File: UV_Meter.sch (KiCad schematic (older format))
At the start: 8 parts, among them SW1 SW_Push, U1 ATtiny85-20PU

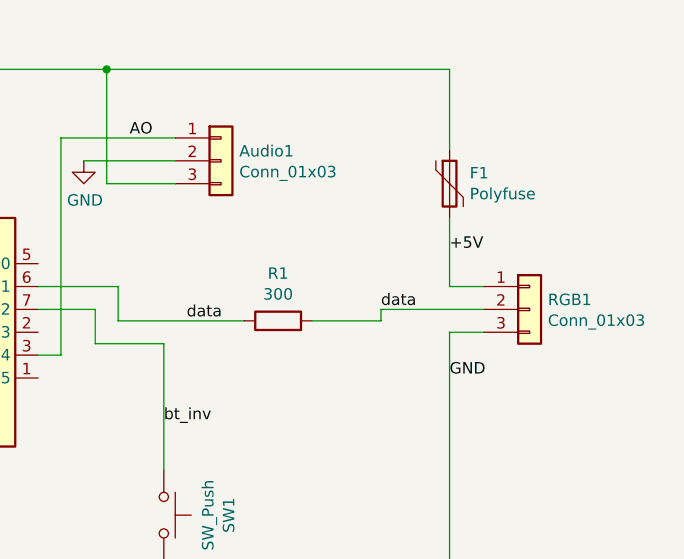
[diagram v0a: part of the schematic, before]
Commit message: switched PWR & LED
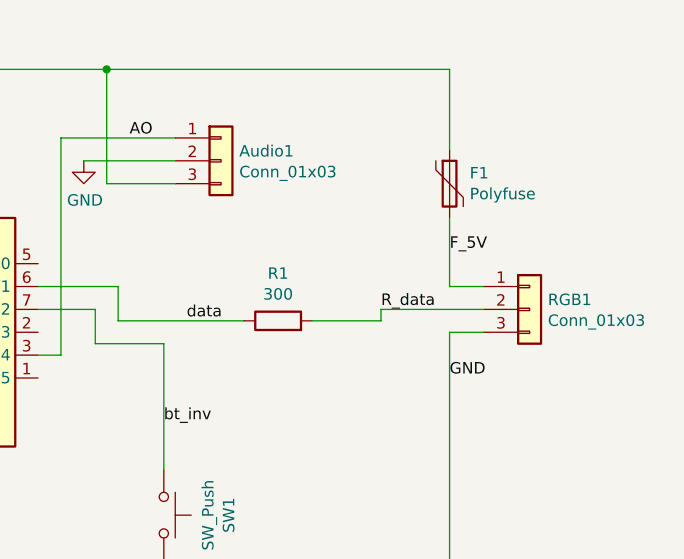
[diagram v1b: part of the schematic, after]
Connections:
- net +5V: no longer F1.2, RGB1.1 (Pin_1)
- net data: no longer R1.2, RGB1.2 (Pin_2)
- new net F_5V: F1.2, RGB1.1 (Pin_1)
- new net R_data: R1.2, RGB1.2 (Pin_2)
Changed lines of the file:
@@
 $EndComp
-Wire Wire Line
-	4550 2650 4850 2650
 Wire Wire Line
 	4850 2650 4850 2600
@@
 	4850 2600 5300 2600
 Text Label 4850 2600 0    50   ~ 0
-data
+R_data
 Text Label 5150 2350 0    50   ~ 0
-+5V
+F_5V
 Text Label 5150 2900 0    50   ~ 0
 GND
@@
 Wire Wire Line
 	5150 2200 5150 2500
-Wire Wire Line
-	5150 1550 5150 1900
 $Comp
 L Device:Polyfuse F1
@@
 	1    0    0    -1
 $EndComp
+Wire Wire Line
+	5150 1550 5150 1900
+Wire Wire Line
+	4850 2650 4550 2650
 $EndSCHEMATC

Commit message: added mounting holes and played around
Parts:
- added H1: MountingHole, MountingHole:MountingHole_3.2mm_M3_ISO14580, symbol Mechanical:MountingHole
- added R_reset1: 10k, Resistor_SMD:R_0603_1608Metric, symbol Device:R
- F_LED1: renamed from F1; value Polyfuse -> 500mA
- renumbered R1 to R_data1
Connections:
- net +5V: now also R_reset1.1
- net reset: now reaches U1.1 (~RESET~/PB5)
- net reset: now also R_reset1.2
- net F_5V renamed fused_5V
- net R_data renamed r_data
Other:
- moved on the sheet: C1
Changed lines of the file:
@@
 $EndComp
 $Comp
-L Device:R R1
+L Device:R R_data1
 U 1 1 5C9F3835
 P 4400 2650
-F 0 "R1" V 4607 2650 50  0000 C CNN
+F 0 "R_data1" V 4607 2650 50  0000 C CNN
 F 1 "300" V 4516 2650 50  0000 C CNN
 F 2 "Resistor_SMD:R_0603_1608Metric" V 4330 2650 50  0001 C CNN
@@
 	4850 2600 5300 2600
 Text Label 4850 2600 0    50   ~ 0
-R_data
+r_data
 Text Label 5150 2350 0    50   ~ 0
-F_5V
+fused_5V
 Text Label 5150 2900 0    50   ~ 0
 GND
 Wire Wire Line
-	5150 1550 3650 1550
-Wire Wire Line
 	5150 2200 5150 2500
 $Comp
-L Device:Polyfuse F1
+L Device:Polyfuse F_LED1
 U 1 1 5CA0A446
 P 5150 2050
-F 0 "F1" H 5238 2096 50  0000 L CNN
-F 1 "Polyfuse" H 5238 2005 50  0000 L CNN
+F 0 "F_LED1" H 5238 2096 50  0000 L CNN
+F 1 "500mA" H 5238 2005 50  0000 L CNN
 F 2 "Fuse:Fuse_1206_3216Metric" H 5200 1850 50  0001 L CNN
 F 3 "~" H 5150 2050 50  0001 C CNN
@@
 	1900 3400 2750 3400
 Wire Wire Line
-	1900 2450 1900 3400
-Wire Wire Line
-	1900 2150 1900 2050
+	1900 2650 1900 3400
+Wire Wire Line
+	1900 2350 1900 2050
 Wire Wire Line
 	1900 2050 2750 2050
@@
 bt_inv
 Wire Wire Line
-	3700 2650 4250 2650
+	3900 2650 4250 2650
 Text Label 4000 2650 0    50   ~ 0
 data
-Text Label 3750 1850 0    50   ~ 0
-AO
-$Comp
-L power:GND #PWR0103
-U 1 1 5CA39264
-P 3550 1950
-F 0 "#PWR0103" H 3550 1700 50  0001 C CNN
-F 1 "GND" H 3555 1777 50  0000 C CNN
-F 2 "" H 3550 1950 50  0001 C CNN
-F 3 "" H 3550 1950 50  0001 C CNN
-	1    3550 1950
-	1    0    0    -1
-$EndComp
-Wire Wire Line
-	3950 1950 3550 1950
-Wire Wire Line
-	3950 2050 3650 2050
-Wire Wire Line
-	3650 2050 3650 1550
-Connection ~ 3650 1550
-Wire Wire Line
-	3650 1550 2750 1550
-Wire Wire Line
-	3350 2800 3450 2800
-Wire Wire Line
-	3450 2800 3450 1850
-Wire Wire Line
-	3450 1850 3950 1850
+Wire Wire Line
+	3350 2800 3700 2800
 $Comp
 L Device:C C1
 U 1 1 5C9F146E
-P 1900 2300
-F 0 "C1" H 2015 2346 50  0000 L CNN
-F 1 "100u" H 2015 2255 50  0000 L CNN
-F 2 "Capacitor_THT:CP_Radial_D7.5mm_P2.50mm" H 1938 2150 50  0001 C CNN
-F 3 "~" H 1900 2300 50  0001 C CNN
-	1    1900 2300
+P 1900 2500
+F 0 "C1" H 2015 2546 50  0000 L CNN
+F 1 "100u" H 2015 2455 50  0000 L CNN
+F 2 "Capacitor_THT:CP_Radial_D7.5mm_P2.50mm" H 1938 2350 50  0001 C CNN
+F 3 "~" H 1900 2500 50  0001 C CNN
+	1    1900 2500
 	1    0    0    -1
 $EndComp
@@
 	1450 2750 1450 4000
 Wire Wire Line
-	3700 2500 3350 2500
-Wire Wire Line
-	3700 2500 3700 2650
-Wire Wire Line
-	3350 2600 3600 2600
-Wire Wire Line
-	3600 2600 3600 2750
-Wire Wire Line
-	3600 2750 3900 2750
+	3900 2500 3350 2500
+Wire Wire Line
+	3900 2500 3900 2650
+Wire Wire Line
+	3350 2600 3800 2600
+Wire Wire Line
+	3800 2600 3800 2750
+Wire Wire Line
+	3800 2750 3900 2750
 Wire Wire Line
 	3900 2750 3900 3300
+Wire Wire Line
+	5150 1550 5150 1900
+Wire Wire Line
+	4850 2650 4550 2650
+$Comp
+L Device:R R_reset1
+U 1 1 5CA11B10
+P 3100 2050
+F 0 "R_reset1" V 3307 2050 50  0000 C CNN
+F 1 "10k" V 3216 2050 50  0000 C CNN
+F 2 "Resistor_SMD:R_0603_1608Metric" V 3030 2050 50  0001 C CNN
+F 3 "~" H 3100 2050 50  0001 C CNN
+	1    3100 2050
+	0    -1   -1   0
+$EndComp
+Wire Wire Line
+	2750 2050 2950 2050
+Wire Wire Line
+	3250 2050 3450 2050
+Wire Wire Line
+	3450 2050 3450 2900
+Wire Wire Line
+	3450 2900 3350 2900
+Connection ~ 3900 1550
+Wire Wire Line
+	3900 1550 2750 1550
+Wire Wire Line
+	5150 1550 3900 1550
 $Comp
 L Connector_Generic:Conn_01x03 Audio1
@@
 $EndComp
 Wire Wire Line
-	5150 1550 5150 1900
-Wire Wire Line
-	4850 2650 4550 2650
+	3700 1850 3950 1850
+Wire Wire Line
+	3700 2800 3700 1850
+Wire Wire Line
+	3900 2050 3900 1550
+Wire Wire Line
+	3950 2050 3900 2050
+Wire Wire Line
+	3950 1950 3750 1950
+$Comp
+L power:GND #PWR0103
+U 1 1 5CA39264
+P 3750 1950
+F 0 "#PWR0103" H 3750 1700 50  0001 C CNN
+F 1 "GND" H 3755 1777 50  0000 C CNN
+F 2 "" H 3750 1950 50  0001 C CNN
+F 3 "" H 3750 1950 50  0001 C CNN
+	1    3750 1950
+	1    0    0    -1
+$EndComp
+Text Label 3750 1850 0    50   ~ 0
+AO
+Text Label 3350 2050 0    50   ~ 0
+reset
+$Comp
+L Mechanical:MountingHole H1
+U 1 1 5CA3BE5F
+P 5250 1300
+F 0 "H1" H 5350 1346 50  0000 L CNN
+F 1 "MountingHole" H 5350 1255 50  0000 L CNN
+F 2 "MountingHole:MountingHole_3.2mm_M3_ISO14580" H 5250 1300 50  0001 C CNN
+F 3 "~" H 5250 1300 50  0001 C CNN
+	1    5250 1300
+	1    0    0    -1
+$EndComp
 $EndSCHEMATC

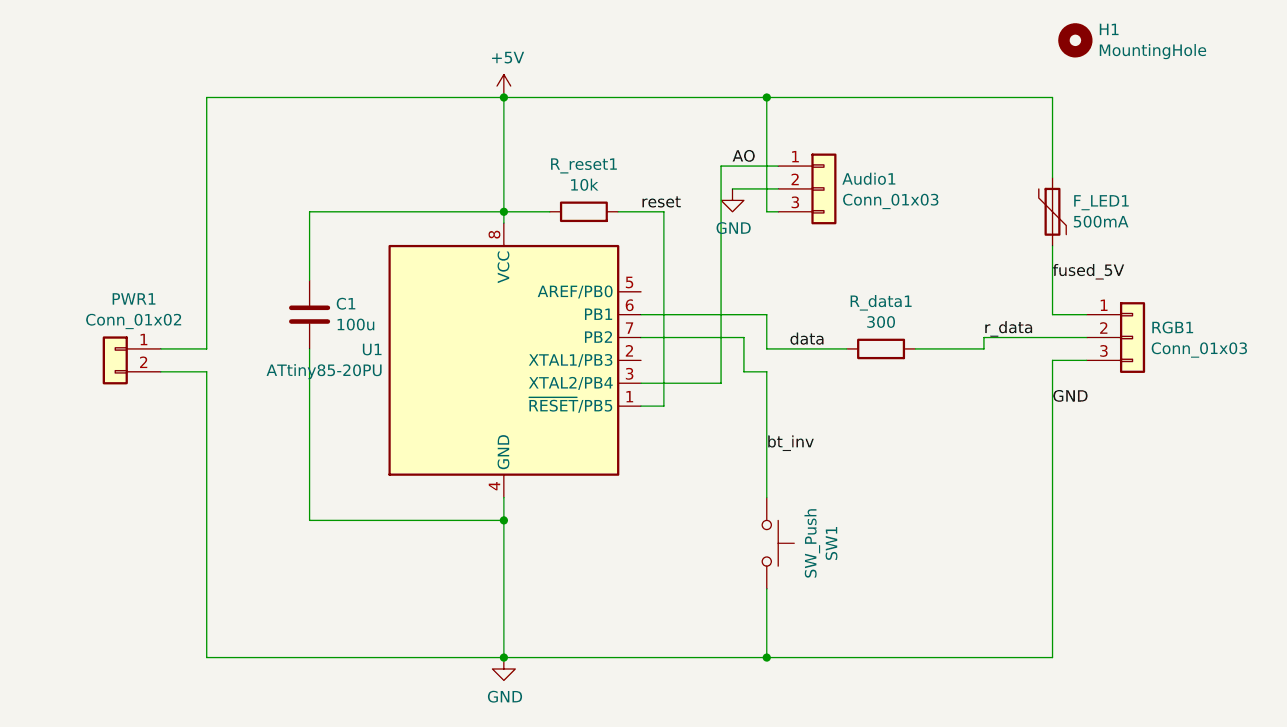
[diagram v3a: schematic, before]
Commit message: added 100nF ceramic, streamlined reset
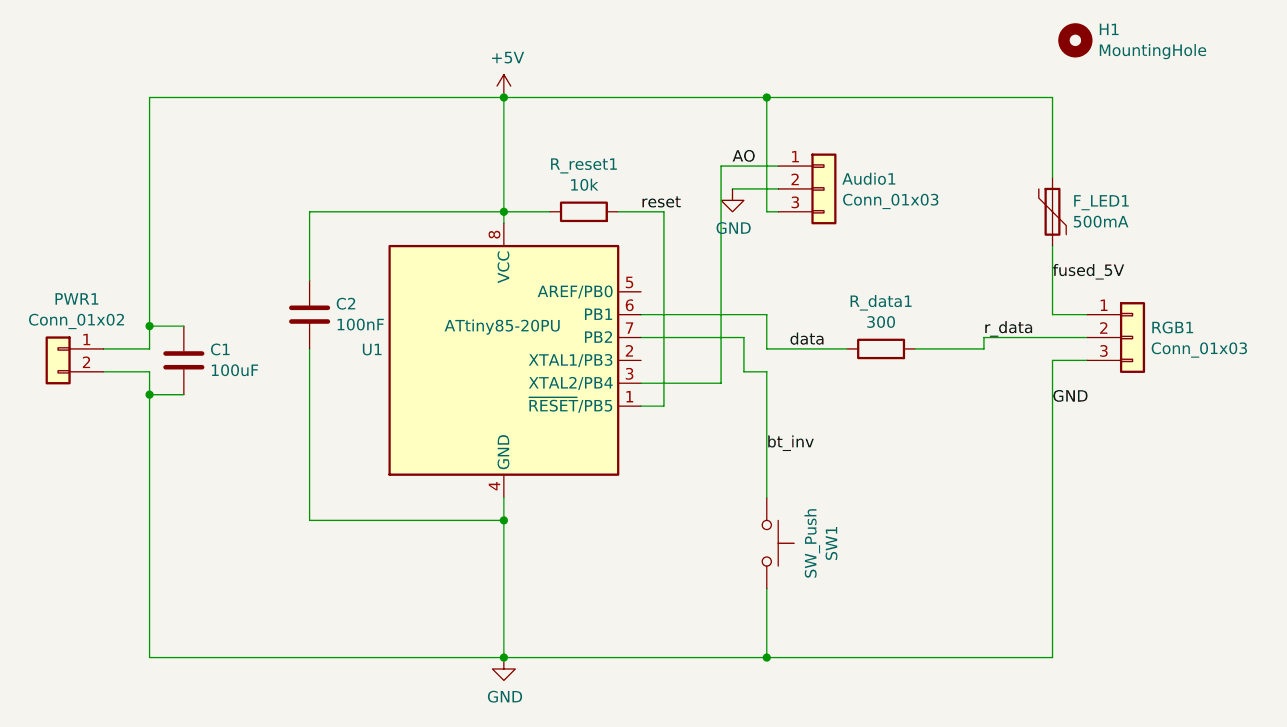
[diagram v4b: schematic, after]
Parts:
- added C2: 100nF, Capacitor_SMD:C_0603_1608Metric, symbol Device:C
- C1: value 100u -> 100uF
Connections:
- net +5V: now also C2.1
- net GND: now also C2.2
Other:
- moved on the sheet: C1, PWR1
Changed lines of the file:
@@
 P 2750 2700
 F 0 "U1" H 2221 2746 50  0000 R CNN
-F 1 "ATtiny85-20PU" H 2221 2655 50  0000 R CNN
+F 1 "ATtiny85-20PU" H 3000 2850 50  0000 R CNN
 F 2 "Package_DIP:DIP-8_W7.62mm" H 2750 2700 50  0001 C CIN
 F 3 "http://ww1.microchip.com/downloads/en/DeviceDoc/atmel-2586-avr-8-bit-microcontroller-attiny25-attiny45-attiny85_datasheet.pdf" H 2750 2700 50  0001 C CNN
@@
 $EndComp
 Wire Wire Line
-	1450 1550 2750 1550
-Wire Wire Line
-	1450 4000 2750 4000
+	1200 1550 2750 1550
+Wire Wire Line
+	1200 4000 2750 4000
 $Comp
 L Connector_Generic:Conn_01x02 PWR1
 U 1 1 5CA1BCB0
-P 1050 2650
-F 0 "PWR1" H 968 2867 50  0000 C CNN
-F 1 "Conn_01x02" H 968 2776 50  0000 C CNN
-F 2 "Connector_PinHeader_2.54mm:PinHeader_1x02_P2.54mm_Vertical" H 1050 2650 50  0001 C CNN
-F 3 "~" H 1050 2650 50  0001 C CNN
-	1    1050 2650
+P 800 2650
+F 0 "PWR1" H 718 2867 50  0000 C CNN
+F 1 "Conn_01x02" H 718 2776 50  0000 C CNN
+F 2 "Connector_PinHeader_2.54mm:PinHeader_1x02_P2.54mm_Vertical" H 800 2650 50  0001 C CNN
+F 3 "~" H 800 2650 50  0001 C CNN
+	1    800  2650
 	-1   0    0    -1
 $EndComp
 Wire Wire Line
-	1250 2650 1450 2650
-Wire Wire Line
-	1250 2750 1450 2750
+	1000 2650 1200 2650
+Wire Wire Line
+	1000 2750 1200 2750
 Text Label 3900 3100 0    50   ~ 0
 bt_inv
@@
 L Device:C C1
 U 1 1 5C9F146E
-P 1900 2500
-F 0 "C1" H 2015 2546 50  0000 L CNN
-F 1 "100u" H 2015 2455 50  0000 L CNN
-F 2 "Capacitor_THT:CP_Radial_D7.5mm_P2.50mm" H 1938 2350 50  0001 C CNN
-F 3 "~" H 1900 2500 50  0001 C CNN
-	1    1900 2500
-	1    0    0    -1
-$EndComp
-Wire Wire Line
-	1450 1550 1450 2650
-Wire Wire Line
-	1450 2750 1450 4000
+P 1350 2700
+F 0 "C1" H 1465 2746 50  0000 L CNN
+F 1 "100uF" H 1465 2655 50  0000 L CNN
+F 2 "Capacitor_THT:CP_Radial_D7.5mm_P2.50mm" H 1388 2550 50  0001 C CNN
+F 3 "~" H 1350 2700 50  0001 C CNN
+	1    1350 2700
+	1    0    0    -1
+$EndComp
+Wire Wire Line
+	1200 1550 1200 2550
+Wire Wire Line
+	1200 2750 1200 2850
 Wire Wire Line
 	3900 2500 3350 2500
@@
 	0    -1   -1   0
 $EndComp
+$Comp
+L Device:C C2
+U 1 1 5CC2270E
+P 1900 2500
+F 0 "C2" H 2015 2546 50  0000 L CNN
+F 1 "100nF" H 2015 2455 50  0000 L CNN
+F 2 "Capacitor_SMD:C_0603_1608Metric" H 1938 2350 50  0001 C CNN
+F 3 "~" H 1900 2500 50  0001 C CNN
+	1    1900 2500
+	1    0    0    -1
+$EndComp
+Wire Wire Line
+	1350 2850 1200 2850
+Connection ~ 1200 2850
+Wire Wire Line
+	1200 2850 1200 4000
+Wire Wire Line
+	1350 2550 1200 2550
+Connection ~ 1200 2550
+Wire Wire Line
+	1200 2550 1200 2650
 $EndSCHEMATC

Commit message: added version, name; improved connector to horizontal
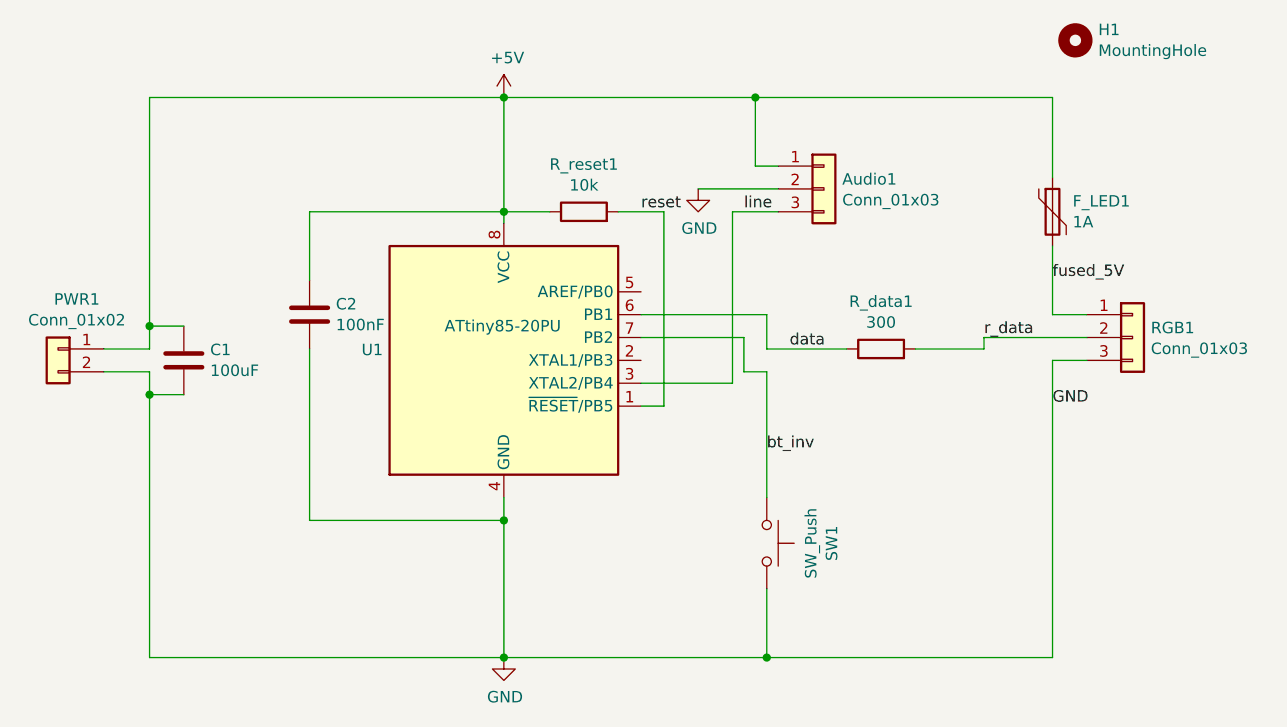
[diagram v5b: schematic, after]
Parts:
- Audio1: footprint Connector_PinSocket_2.54mm:PinSocket_1x03_P2.54mm_Vertical -> Connector_PinSocket_2.54mm:PinSocket_1x03_P2.54mm_Horizontal
- C1: footprint Capacitor_THT:CP_Radial_D7.5mm_P2.50mm -> Capacitor_THT:CP_Radial_D5.0mm_P2.50mm
- F_LED1: value 500mA -> 1A
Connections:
- net +5V: now also Audio1.1 (Pin_1); no longer Audio1.3 (Pin_3)
- net AO renamed line
- net line: now also Audio1.3 (Pin_3); no longer Audio1.1 (Pin_1)
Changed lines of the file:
@@
 P 5150 2050
 F 0 "F_LED1" H 5238 2096 50  0000 L CNN
-F 1 "500mA" H 5238 2005 50  0000 L CNN
+F 1 "1A" H 5238 2005 50  0000 L CNN
 F 2 "Fuse:Fuse_1206_3216Metric" H 5200 1850 50  0001 L CNN
 F 3 "~" H 5150 2050 50  0001 C CNN
@@
 bt_inv
 Wire Wire Line
-	3350 2800 3700 2800
+	3350 2800 3750 2800
 $Comp
 L Device:C C1
@@
 F 0 "C1" H 1465 2746 50  0000 L CNN
 F 1 "100uF" H 1465 2655 50  0000 L CNN
-F 2 "Capacitor_THT:CP_Radial_D7.5mm_P2.50mm" H 1388 2550 50  0001 C CNN
+F 2 "Capacitor_THT:CP_Radial_D5.0mm_P2.50mm" H 1388 2550 50  0001 C CNN
 F 3 "~" H 1350 2700 50  0001 C CNN
 	1    1350 2700
@@
 Wire Wire Line
 	3450 2900 3350 2900
-Connection ~ 3900 1550
-Wire Wire Line
-	3900 1550 2750 1550
-Wire Wire Line
-	5150 1550 3900 1550
 $Comp
 L Connector_Generic:Conn_01x03 Audio1
@@
 F 0 "Audio1" H 4230 1992 50  0000 L CNN
 F 1 "Conn_01x03" H 4230 1901 50  0000 L CNN
-F 2 "Connector_PinSocket_2.54mm:PinSocket_1x03_P2.54mm_Vertical" H 4150 1950 50  0001 C CNN
+F 2 "Connector_PinSocket_2.54mm:PinSocket_1x03_P2.54mm_Horizontal" H 4150 1950 50  0001 C CNN
 F 3 "~" H 4150 1950 50  0001 C CNN
 	1    4150 1950
@@
 $EndComp
 Wire Wire Line
-	3700 1850 3950 1850
+	3750 2800 3750 2050
 Wire Wire Line
-	3700 2800 3700 1850
-Wire Wire Line
-	3900 2050 3900 1550
-Wire Wire Line
-	3950 2050 3900 2050
-Wire Wire Line
-	3950 1950 3750 1950
+	3950 1950 3600 1950
 $Comp
 L power:GND #PWR0103
 U 1 1 5CA39264
-P 3750 1950
-F 0 "#PWR0103" H 3750 1700 50  0001 C CNN
-F 1 "GND" H 3755 1777 50  0000 C CNN
-F 2 "" H 3750 1950 50  0001 C CNN
-F 3 "" H 3750 1950 50  0001 C CNN
-	1    3750 1950
+P 3600 1950
+F 0 "#PWR0103" H 3600 1700 50  0001 C CNN
+F 1 "GND" H 3605 1777 50  0000 C CNN
+F 2 "" H 3600 1950 50  0001 C CNN
+F 3 "" H 3600 1950 50  0001 C CNN
+	1    3600 1950
 	1    0    0    -1
 $EndComp
-Text Label 3750 1850 0    50   ~ 0
-AO
+Text Label 3800 2050 0    50   ~ 0
+line
 Text Label 3350 2050 0    50   ~ 0
 reset
@@
 Wire Wire Line
 	1200 2550 1200 2650
+Wire Wire Line
+	2750 1550 3850 1550
+Wire Wire Line
+	3950 1850 3850 1850
+Wire Wire Line
+	3850 1850 3850 1550
+Connection ~ 3850 1550
+Wire Wire Line
+	3850 1550 5150 1550
+Wire Wire Line
+	3950 2050 3750 2050
 $EndSCHEMATC

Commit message: noted wrong polarity, moved SMD to backside
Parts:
- C1: footprint Capacitor_THT:CP_Radial_D5.0mm_P2.50mm -> Capacitor_THT:CP_Radial_D4.0mm_P2.00mm
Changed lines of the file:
@@
 F 0 "C1" H 1465 2746 50  0000 L CNN
 F 1 "100uF" H 1465 2655 50  0000 L CNN
-F 2 "Capacitor_THT:CP_Radial_D5.0mm_P2.50mm" H 1388 2550 50  0001 C CNN
+F 2 "Capacitor_THT:CP_Radial_D4.0mm_P2.00mm" H 1388 2550 50  0001 C CNN
 F 3 "~" H 1350 2700 50  0001 C CNN
 	1    1350 2700
